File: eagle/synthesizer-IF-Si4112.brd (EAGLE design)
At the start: 34 x 31 mm, 34 parts, among them J1 142-0701-851, J3 142-0701-851, U1 SI4112, X1 ECS-TXO-3225

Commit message: Si4112 layout finish
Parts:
- renumbered R10 to JP6
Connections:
- net N$19 renamed VCTRL
- net N$4 renamed /PWDN
- net N$5 renamed /SEN
- net N$6 renamed SCLK
- net N$7 renamed SDATA
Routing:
- net GND: track 0.00 -> 68.1 mm, vias 2 -> 159
- net VCTRL: track 5.08 -> 13.7 mm
- net +3V3: track 5.20 -> 8.17 mm, vias 14 -> 17
- net N$10: track 6.42 -> 8.85 mm
- added copper zone on layer 1, net +3V3
- added copper zone on layer 1, net REF_IN
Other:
- outline, holes or cut-outs redrawn
- board text added: "+"
- board text added: "-"
- board text added: "/PWDN"
- board text added: "3V3"
- board text added: "AUX"
- board text added: "CK"
- board text added: "DA"
- board text added: "EN"
- board text added: "IF Synthesizer Si4112 808 MHz L band LO PSAS / OreSat 2019-09-11 v1.0 E.M. - KJ7AOG"
- board text added: "IF-OUT"
- board text added: "PWR"
- board text added: "REF-IN"
- board text added: "VCTRL"

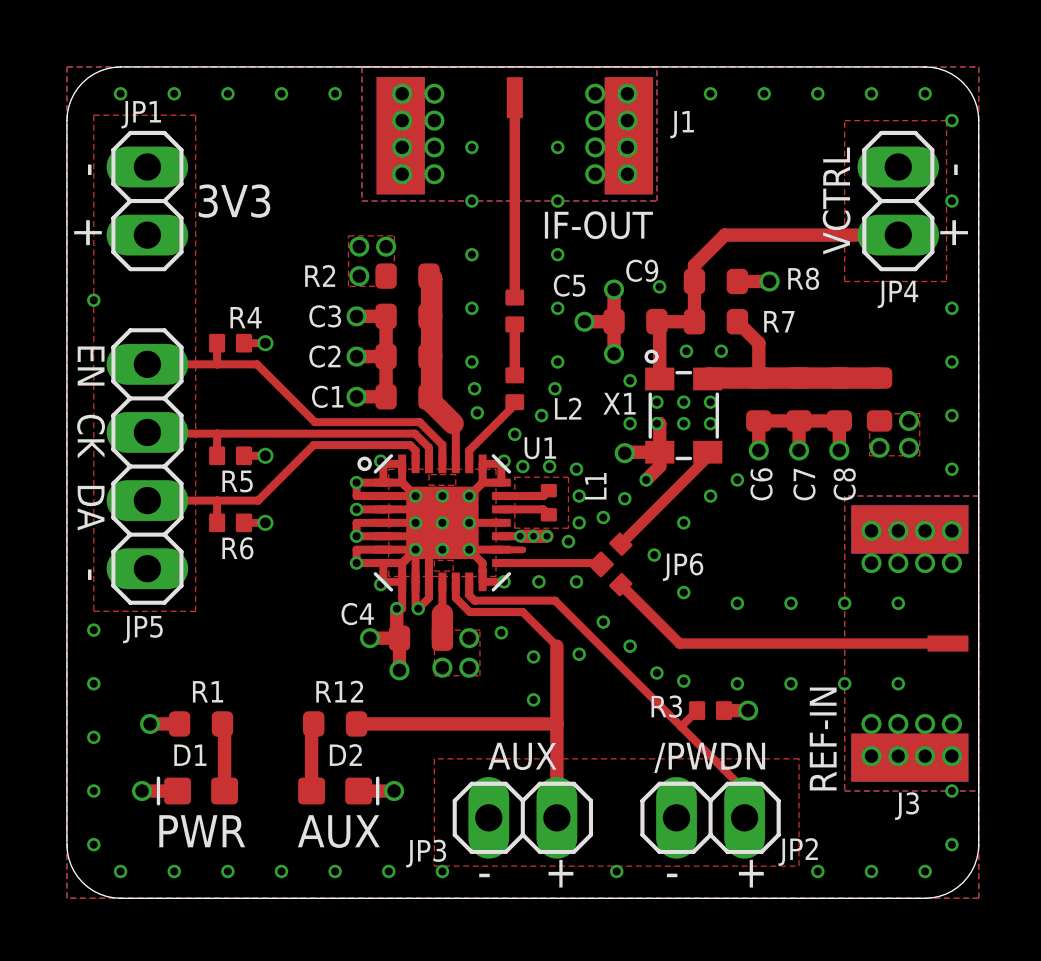
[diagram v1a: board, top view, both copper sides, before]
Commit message: Si4112, added better shutdown control
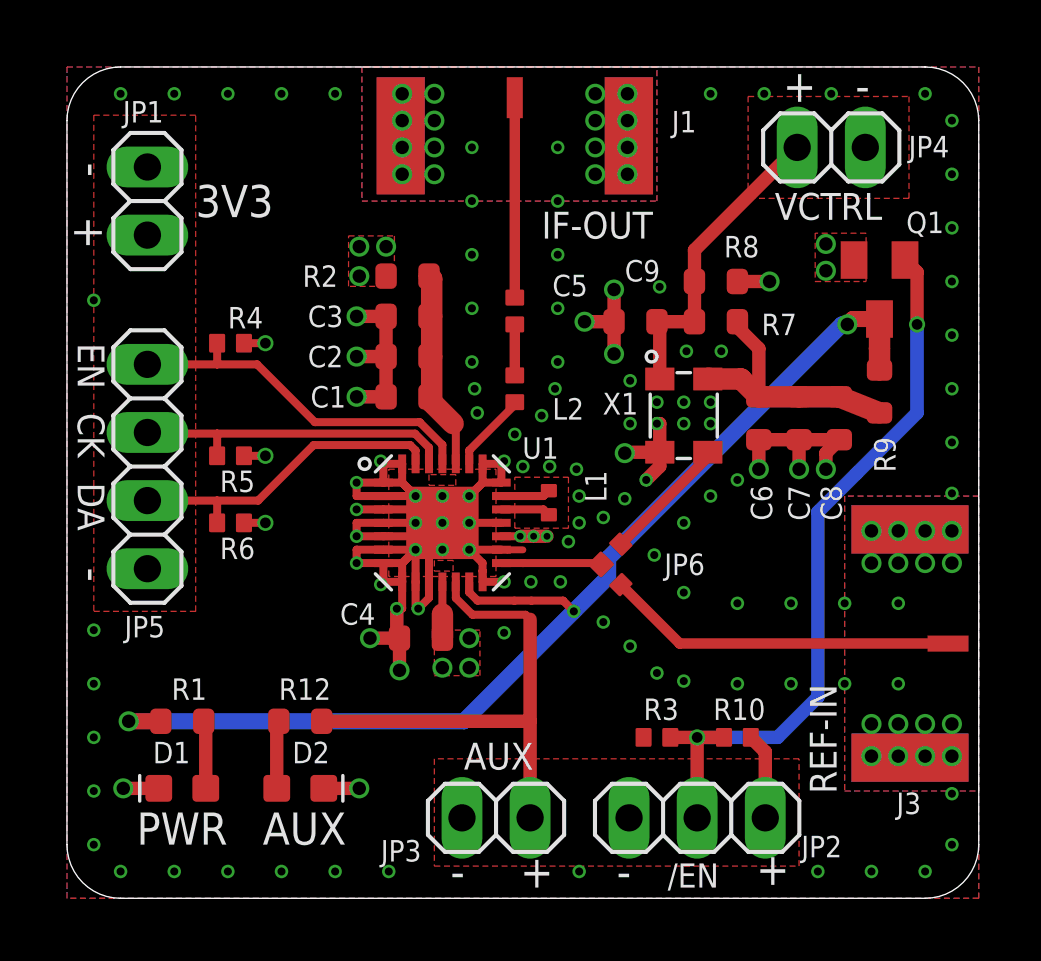
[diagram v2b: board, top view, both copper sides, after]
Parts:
- added Q1: PMOS, transistor-small-signal:SOT23
- added R10: NP, oresat-rcl:.0402-B-NOSILK
- JP2: device pinhead:1X02 -> pinhead:1X03
- R3: value 47k -> NP
- moved JP4 3.20 mm to (28.5, 28.0), turned to 180 degrees
- moved R3 2.24 mm to (22.0, 6.00)
- moved D2 1.30 mm to (8.70, 4.10)
- moved R12 1.30 mm to (8.70, 6.60)
- moved JP3 1.00 mm to (16.0, 3.00)
- moved D1 0.71 mm to (4.30, 4.10)
- moved R1 0.71 mm to (4.30, 6.60)
- moved C6 0.70 mm to (25.8, 17.9)
- moved C7 0.70 mm to (27.3, 17.9)
- moved C8 0.70 mm to (28.8, 17.9)
- moved JP2 0.50 mm to (23.5, 3.00)
- moved R9 0.30 mm to (30.3, 18.9), turned to 270 degrees
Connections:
- removed net /PWDN: JP2.2, R3.1, U1.13
- new net N$4: JP2.2, Q1.1, R10.1, R3.2
- new net N$5: Q1.3, R1.2, R9.1, U1.13
- net +3V3: now also JP2.3, Q1.2, R10.2; no longer R1.2, R3.2, R9.1
- net GND: now also R3.1
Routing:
- net N$5: track 0.00 -> 42.3 mm, vias 0 -> 3
- net N$4: track 0.00 -> 28.1 mm, vias 0 -> 2
- net /PWDN: track 15.7 -> 0.00 mm
- net VCTRL: track 13.7 -> 11.7 mm
- net +3V3: track 8.17 -> 9.40 mm, vias 17 -> 14
- net N$10: track 8.85 -> 9.98 mm
- net GND: track 68.1 -> 68.3 mm, vias 159 -> 156
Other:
- board text added: "/EN"
- board text removed: "/PWDN"

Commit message: Si4112, fix shutdown control and add bkup power down battery option
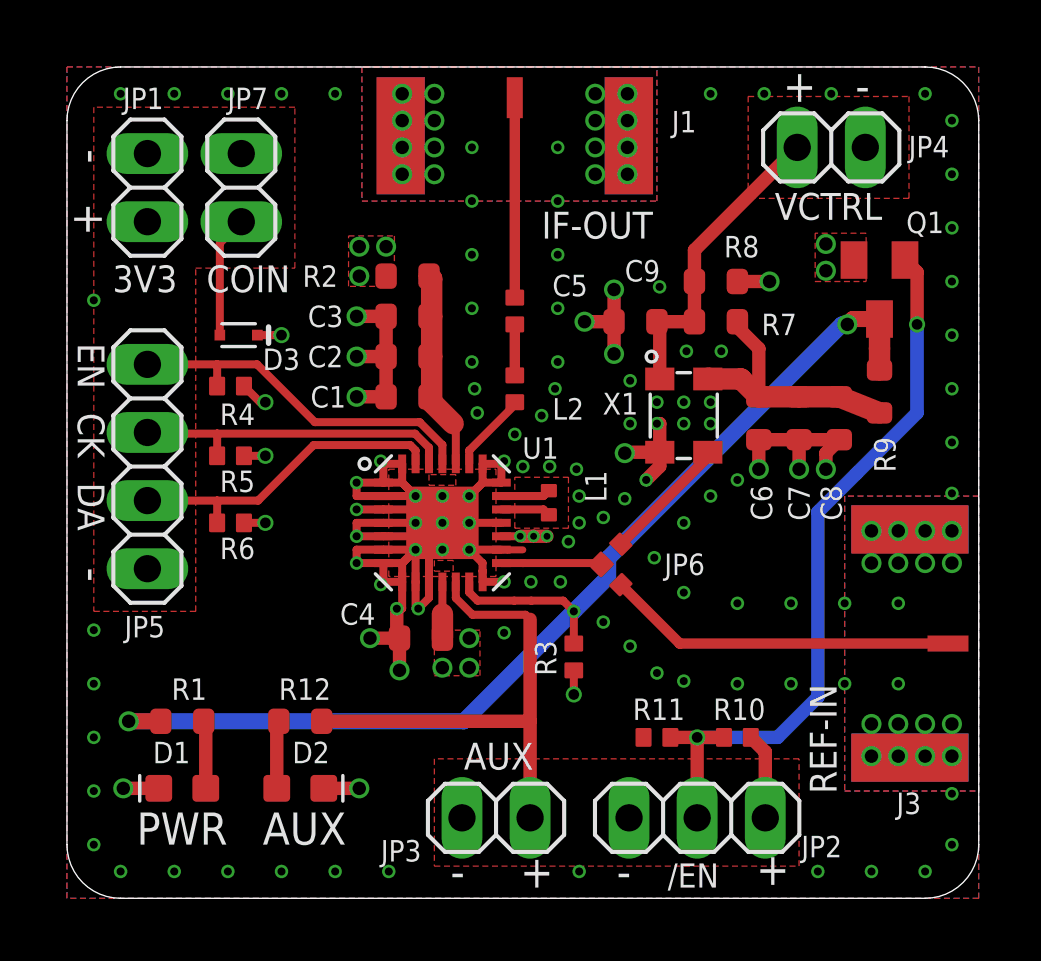
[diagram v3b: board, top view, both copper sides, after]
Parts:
- added D3: 120mA/40V/370mV, SparkFun-DiscreteSemi:SOD-523
- added JP7: (no value), pinhead:1X02
- added R99: NP, oresat-rcl:.0402-B-NOSILK
- R3: value NP -> 47k
- moved R11 6.28 mm to (22.0, 6.00), turned to 0 degrees
- moved R3 4.31 mm to (18.9, 9.00), turned to 90 degrees
- moved R4 1.60 mm to (6.10, 19.1)
- moved JP1 0.50 mm to (3.00, 26.5)
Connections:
- new net N$1: D3.A, JP7.2
- net +3V3: now also D3.C
- net GND: now also JP7.1, R11.1
- net N$4: now also R11.2; no longer R3.2
- net N$5: now also R3.2
- net REF_IN: now also R99.2; no longer R11.2
- net XIN: now also R99.1; no longer R11.1
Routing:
- net N$1: track 0.00 -> 4.56 mm
- net N$5: track 42.3 -> 43.5 mm
- net +3V3: track 9.40 -> 10.5 mm, vias 14 -> 15
- net GND: track 68.3 -> 69.2 mm, vias 156 -> 157
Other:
- board text added: "COIN"
- board text added: "D3"
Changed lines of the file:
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@@
 <text x="22.4" y="0.4" size="0.9" layer="21" font="vector" ratio="15">/EN</text>
 <text x="30.4" y="26.3" size="1" layer="21" font="vector" ratio="15" rot="R180">VCTRL</text>
-<text x="4.8" y="25.4" size="1.2" layer="21" font="vector" ratio="15">3V3</text>
+<text x="1.7" y="22.6" size="1" layer="21" font="vector" ratio="15">3V3</text>
 <text x="17.7" y="24.6" size="1" layer="21" font="vector" ratio="15">IF-OUT</text>
 <text x="28.7" y="3.9" size="1" layer="21" font="vector" ratio="15" rot="R90">REF-IN</text>
@@
 <text x="26.7" y="29.7" size="1.2" layer="21" font="vector" ratio="15">+</text>
 <text x="29.4" y="29.7" size="1.2" layer="21" font="vector" ratio="15">-</text>
-<text x="1.3" y="24.2" size="1.2" layer="21" font="vector" ratio="15" rot="R90">+</text>
-<text x="1.3" y="26.9" size="1.2" layer="21" font="vector" ratio="15" rot="R90">-</text>
+<text x="1.3" y="24.7" size="1.2" layer="21" font="vector" ratio="15" rot="R90">+</text>
+<text x="1.3" y="27.4" size="1.2" layer="21" font="vector" ratio="15" rot="R90">-</text>
 <text x="1.3" y="11.8" size="1.2" layer="21" font="vector" ratio="15" rot="R90">-</text>
 <text x="0.4" y="20.7" size="1" layer="21" font="vector" ratio="15" rot="SR270">EN</text>
@@
 2019-09-11  v1.0
 E.M. - KJ7AOG</text>
+<text x="7.3" y="19.7" size="0.8" layer="21" font="vector" ratio="15">D3</text>
+<text x="5.2" y="22.6" size="1" layer="21" font="vector" ratio="15">COIN</text>
 </plain>
 <attributes>
@@
 <attribute name="NAME" x="31.85" y="3.94" size="0.8" layer="25" font="vector" ratio="15" rot="R180"/>
 </element>
-<element name="JP1" library="pinhead" library_urn="urn:adsk.eagle:library:325" package="1X02" package3d_urn="urn:adsk.eagle:package:22435/2" value="" x="3" y="26" smashed="yes" rot="R270">
-<attribute name="NAME" x="2.0838" y="28.9288" size="0.8" layer="25" font="vector" ratio="15"/>
-<attribute name="POPULARITY" value="98" x="-13.51" y="-8.29" size="1.778" layer="27" rot="R270" display="off"/>
-<attribute name="VALUE" x="-0.175" y="28.54" size="1.27" layer="27" rot="R270"/>
+<element name="JP1" library="pinhead" library_urn="urn:adsk.eagle:library:325" package="1X02" package3d_urn="urn:adsk.eagle:package:22435/2" value="" x="3" y="26.5" smashed="yes" rot="R270">
+<attribute name="NAME" x="2.0838" y="29.4288" size="0.8" layer="25" font="vector" ratio="15"/>
+<attribute name="POPULARITY" value="98" x="-13.51" y="-7.79" size="1.778" layer="27" rot="R270" display="off"/>
+<attribute name="VALUE" x="-0.175" y="29.04" size="1.27" layer="27" rot="R270"/>
 </element>
 <element name="JP2" library="pinhead" library_urn="urn:adsk.eagle:library:325" package="1X03" package3d_urn="urn:adsk.eagle:package:22458/2" value="" x="23.5" y="3" smashed="yes">
@@
 <attribute name="NAME" x="20.3" y="12.85" size="0.2" layer="33" ratio="15" rot="R45" align="center"/>
 </element>
-<element name="R11" library="oresat-rcl" package=".0402-B-NOSILK" value="NP" x="20.3" y="12.05" smashed="yes" rot="R315">
+<element name="R99" library="oresat-rcl" package=".0402-B-NOSILK" value="NP" x="20.3" y="12.05" smashed="yes" rot="R315">
 <attribute name="NAME" x="20.3" y="12.05" size="0.2" layer="33" ratio="15" rot="R315" align="center"/>
 </element>
@@
 <attribute name="NAME" x="12.7" y="23.2" size="0.3" layer="33" ratio="15" rot="R180" align="center"/>
 </element>
-<element name="R3" library="oresat-rcl" package=".0402-B-NOSILK" value="NP" x="22" y="6" smashed="yes">
-<attribute name="NAME" x="21.5" y="6.65" size="0.8" layer="25" font="vector" ratio="15"/>
+<element name="R11" library="oresat-rcl" package=".0402-B-NOSILK" value="NP" x="22" y="6" smashed="yes">
+<attribute name="NAME" x="21.1" y="6.65" size="0.8" layer="25" font="vector" ratio="15"/>
 <attribute name="NAME" x="22" y="6" size="0.2" layer="33" ratio="15" align="center"/>
 </element>
-<element name="R4" library="oresat-rcl" package=".0402-B-NOSILK" value="47k" x="6.1" y="20.7" smashed="yes">
-<attribute name="NAME" x="6" y="21.25" size="0.8" layer="25" font="vector" ratio="15"/>
-<attribute name="NAME" x="6.1" y="20.7" size="0.2" layer="33" ratio="15" align="center"/>
+<element name="R4" library="oresat-rcl" package=".0402-B-NOSILK" value="47k" x="6.1" y="19.1" smashed="yes">
+<attribute name="NAME" x="5.7" y="17.65" size="0.8" layer="25" font="vector" ratio="15"/>
+<attribute name="NAME" x="6.1" y="19.1" size="0.2" layer="33" ratio="15" align="center"/>
 </element>
 <element name="R5" library="oresat-rcl" package=".0402-B-NOSILK" value="47k" x="6.1" y="16.5" smashed="yes">
@@
 <attribute name="NAME" x="24.1" y="6.65" size="0.8" layer="25" font="vector" ratio="15"/>
 <attribute name="NAME" x="25" y="6" size="0.2" layer="33" ratio="15" align="center"/>
+</element>
+<element name="JP7" library="pinhead" library_urn="urn:adsk.eagle:library:325" package="1X02" package3d_urn="urn:adsk.eagle:package:22435/2" value="" x="6.5" y="26.5" smashed="yes" rot="R270">
+<attribute name="NAME" x="5.9838" y="29.4288" size="0.8" layer="25" font="vector" ratio="15"/>
+<attribute name="POPULARITY" value="98" x="6.5" y="26.5" size="1.778" layer="27" rot="R270" display="off"/>
+<attribute name="VALUE" x="3.325" y="29.04" size="1.27" layer="27" rot="R270"/>
+</element>
+<element name="D3" library="SparkFun-DiscreteSemi" library_urn="urn:adsk.eagle:library:514" package="SOD-523" package3d_urn="urn:adsk.eagle:package:38442/1" value="120mA/40V/370mV" x="6.4" y="21" smashed="yes">
+<attribute name="PROD_ID" value="DIO-11018" x="6.4" y="21" size="1.778" layer="27" display="off"/>
+</element>
+<element name="R3" library="oresat-rcl" package=".0402-B-NOSILK" value="47k" x="18.9" y="9" smashed="yes" rot="R90">
+<attribute name="NAME" x="18.25" y="8.3" size="0.8" layer="25" font="vector" ratio="15" rot="R90"/>
+<attribute name="NAME" x="18.9" y="9" size="0.2" layer="33" ratio="15" rot="R90" align="center"/>
 </element>
 </elements>
@@
 </polygon>
 <polygon width="0.3" layer="1">
-<vertex x="1" y="29.2"/>
+<vertex x="1" y="29.5"/>
 <vertex x="1" y="10.7"/>
 <vertex x="4.8" y="10.7"/>
-<vertex x="4.8" y="29.2"/>
+<vertex x="4.8" y="23.5"/>
+<vertex x="8.5" y="23.5"/>
+<vertex x="8.5" y="29.5"/>
 </polygon>
 <via x="11.3" y="9.7" extent="1-16" drill="0.5"/>
@@
 <via x="24.4" y="20.4" extent="1-16" drill="0.3"/>
 <via x="22.1" y="22.8" extent="1-16" drill="0.3"/>
-<via x="21.9" y="12.8" extent="1-16" drill="0.3"/>
+<via x="21.9" y="12.7" extent="1-16" drill="0.3"/>
 <via x="25" y="15.6" extent="1-16" drill="0.3"/>
 <via x="24" y="15" extent="1-16" drill="0.3"/>
@@
 <via x="12.5" y="29" extent="1-16" drill="0.5"/>
 <via x="12.5" y="30" extent="1-16" drill="0.5"/>
-<contactref element="R3" pad="1"/>
+<contactref element="R11" pad="1"/>
 <via x="33" y="23" extent="1-16" drill="0.3"/>
 <via x="33" y="15.1" extent="1-16" drill="0.3"/>
+<contactref element="JP7" pad="1"/>
+<contactref element="R3" pad="1"/>
+<via x="18.9" y="7.6" extent="1-16" drill="0.4"/>
+<wire x1="18.9" y1="8.5" x2="18.9" y2="7.6" width="0.3" layer="1"/>
 </signal>
 <signal name="/SEN">
@@
 <wire x1="5.6" y1="19.91" x2="7.09" y2="19.91" width="0.3" layer="1"/>
 <wire x1="7.09" y1="19.91" x2="9.246" y2="17.754" width="0.3" layer="1"/>
-<wire x1="5.6" y1="20.7" x2="5.6" y2="19.91" width="0.3" layer="1"/>
+<wire x1="5.6" y1="19.1" x2="5.6" y2="19.91" width="0.3" layer="1"/>
 </signal>
 <signal name="SCLK">
@@
 <signal name="REF_IN" class="1">
 <contactref element="J3" pad="RF1"/>
-<contactref element="R11" pad="2"/>
+<contactref element="R99" pad="2"/>
 <wire x1="20.653553125" y1="11.69644375" x2="22.849996875" y2="9.5" width="0.39" layer="1"/>
 <wire x1="22.849996875" y1="9.5" x2="32.854" y2="9.5" width="0.39" layer="1"/>
@@
 <via x="10.9" y="23.2" extent="1-16" drill="0.5"/>
 <via x="10.9" y="24.3" extent="1-16" drill="0.5"/>
-<via x="7.4" y="20.7" extent="1-16" drill="0.4"/>
+<via x="7.4" y="18.5" extent="1-16" drill="0.4"/>
 <via x="7.4" y="16.5" extent="1-16" drill="0.4"/>
 <via x="7.4" y="14" extent="1-16" drill="0.4"/>
 <wire x1="6.6" y1="14" x2="7.4" y2="14" width="0.3" layer="1"/>
 <wire x1="6.6" y1="16.5" x2="7.4" y2="16.5" width="0.3" layer="1"/>
-<wire x1="6.6" y1="20.7" x2="7.4" y2="20.7" width="0.3" layer="1"/>
 <wire x1="16.2" y1="13.5" x2="16.9" y2="13.5" width="0.3" layer="1"/>
 <via x="16.9" y="13.5" extent="1-16" drill="0.254"/>
@@
 <wire x1="25.5" y1="6" x2="26.04" y2="5.46" width="0.5" layer="1"/>
 <wire x1="26.04" y1="5.46" x2="26.04" y2="3" width="0.5" layer="1"/>
+<contactref element="D3" pad="C"/>
+<wire x1="6.6" y1="19.1" x2="7.2" y2="18.5" width="0.3" layer="1"/>
+<wire x1="7.2" y1="18.5" x2="7.4" y2="18.5" width="0.3" layer="1"/>
+<via x="8" y="21" extent="1-16" drill="0.4"/>
+<wire x1="7.1" y1="21" x2="8" y2="21" width="0.3" layer="1"/>
 </signal>
 <signal name="VCTRL">
@@
 </signal>
 <signal name="XIN" class="2">
-<contactref element="R11" pad="1"/>
+<contactref element="R99" pad="1"/>
 <contactref element="JP6" pad="1"/>
 <contactref element="U1" pad="15"/>
@@
 <signal name="N$4">
 <contactref element="Q1" pad="1"/>
-<contactref element="R3" pad="2"/>
+<contactref element="R11" pad="2"/>
 <contactref element="JP2" pad="2"/>
 <contactref element="R10" pad="1"/>
@@
 <wire x1="18.5" y1="11.1" x2="17.31829375" y2="11.1" width="0.3" layer="1"/>
 <wire x1="15.3082625" y1="11.1" x2="16.68170625" y2="11.1" width="0.3" layer="1"/>
+<contactref element="R3" pad="2"/>
+<wire x1="18.9" y1="9.5" x2="18.9" y2="10.7" width="0.3" layer="1"/>
+</signal>
+<signal name="N$1">
+<contactref element="D3" pad="A"/>
+<contactref element="JP7" pad="2"/>
+<wire x1="6.5" y1="25.23" x2="5.7" y2="24.43" width="0.3" layer="1"/>
+<wire x1="5.7" y1="24.43" x2="5.7" y2="21" width="0.3" layer="1"/>
 </signal>
 </signals>
